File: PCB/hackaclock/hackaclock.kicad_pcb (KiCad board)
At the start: 2 copper layers, 95 x 65 mm, 15 parts, among them J1 Conn_01x08_Pin, SW1 SW_Push, SW2 SW_Push, SW3 SW_Push, SW4 SW_Push, SW5 SW_Push, SW6 SW_Push, U1 XIAO-ESP32-C3-SMD

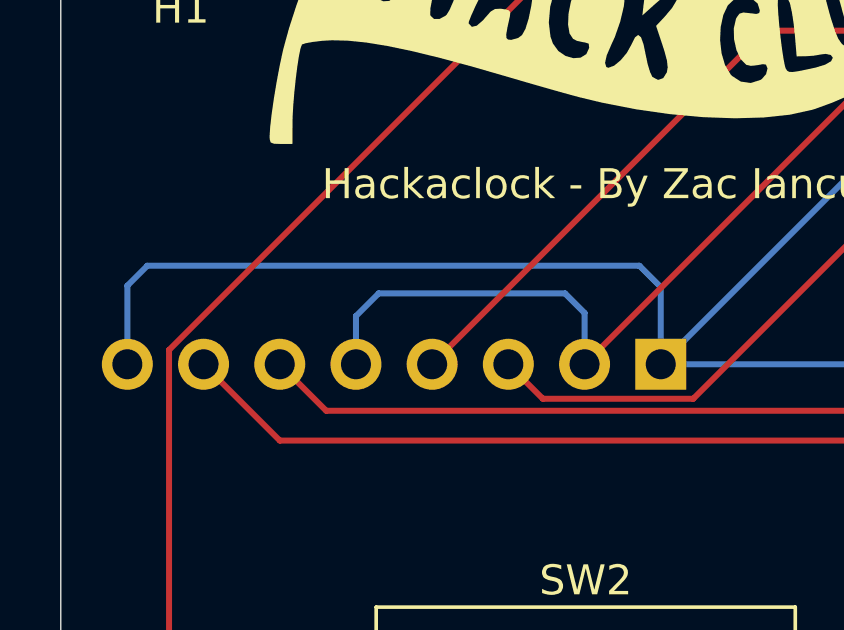
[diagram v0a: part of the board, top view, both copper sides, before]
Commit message: Fix pin connection mistake
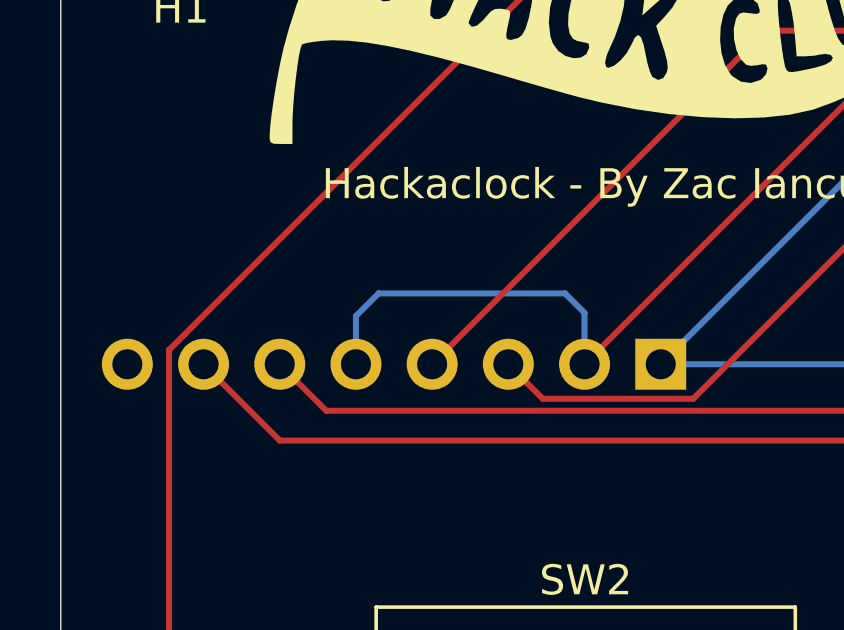
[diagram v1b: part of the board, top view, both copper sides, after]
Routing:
- net GND: track 188.3 -> 164.8 mm
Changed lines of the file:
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@@
 		(sheetname "/")
 		(sheetfile "hackaclock.kicad_sch")
+		(units
+			(unit
+				(name "A")
+				(pins)
+			)
+		)
 		(attr exclude_from_bom)
 		(duplicate_pad_numbers_are_jumpers no)
@@
 		(sheetname "/")
 		(sheetfile "hackaclock.kicad_sch")
+		(units
+			(unit
+				(name "A")
+				(pins)
+			)
+		)
 		(attr exclude_from_bom)
 		(duplicate_pad_numbers_are_jumpers no)
@@
 		(sheetname "/")
 		(sheetfile "hackaclock.kicad_sch")
+		(units
+			(unit
+				(name "A")
+				(pins)
+			)
+		)
 		(attr exclude_from_bom)
 		(duplicate_pad_numbers_are_jumpers no)
@@
 		(sheetname "/")
 		(sheetfile "hackaclock.kicad_sch")
+		(units
+			(unit
+				(name "A")
+				(pins)
+			)
+		)
 		(attr exclude_from_bom)
 		(duplicate_pad_numbers_are_jumpers no)
@@
 		(sheetname "/")
 		(sheetfile "hackaclock.kicad_sch")
+		(units
+			(unit
+				(name "A")
+				(pins "1" "2")
+			)
+		)
 		(attr through_hole)
 		(duplicate_pad_numbers_are_jumpers no)
@@
 		(sheetname "/")
 		(sheetfile "hackaclock.kicad_sch")
+		(units
+			(unit
+				(name "A")
+				(pins "1" "2" "3" "4" "5" "6" "7" "8")
+			)
+		)
 		(attr through_hole)
 		(duplicate_pad_numbers_are_jumpers no)
@@
 		(sheetname "/")
 		(sheetfile "hackaclock.kicad_sch")
+		(units
+			(unit
+				(name "A")
+				(pins "1" "2" "3" "4" "5" "6" "7" "15" "16" "17" "21" "18" "22" "19"
+					"20" "14" "13" "12" "11" "10" "9" "8"
+				)
+			)
+		)
 		(attr smd)
 		(duplicate_pad_numbers_are_jumpers no)
@@
 	)
 	(segment
-		(start 39.289 36.715)
-		(end 40 37.426)
-		(width 0.2)
-		(layer "B.Cu")
-		(net "GND")
-	)
-	(segment
 		(start 40 40)
 		(end 50.04 40)
@@
 	)
 	(segment
-		(start 22.22 37.381)
-		(end 22.886 36.715)
-		(width 0.2)
-		(layer "B.Cu")
-		(net "GND")
-	)
-	(segment
-		(start 22.22 40)
-		(end 22.22 37.381)
-		(width 0.2)
-		(layer "B.Cu")
-		(net "GND")
-	)
-	(segment
 		(start 40.04 50)
 		(end 100.04 50)
@@
 		(width 0.2)
 		(layer "B.Cu")
-		(net "GND")
-	)
-	(segment
-		(start 22.886 36.715)
-		(end 39.289 36.715)
-		(width 0.2)
-		(layer "B.Cu")
-		(net "GND")
-	)
-	(segment
-		(start 40 37.426)
-		(end 40 40)
-		(width 0.2)
-		(layer "B.Cu")
